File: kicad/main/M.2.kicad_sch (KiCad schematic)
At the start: 10 parts, among them J2 1-2199119-5, M2_ACT1 YLED0603B, Y1 ASEK-32.768KHZ-LRT

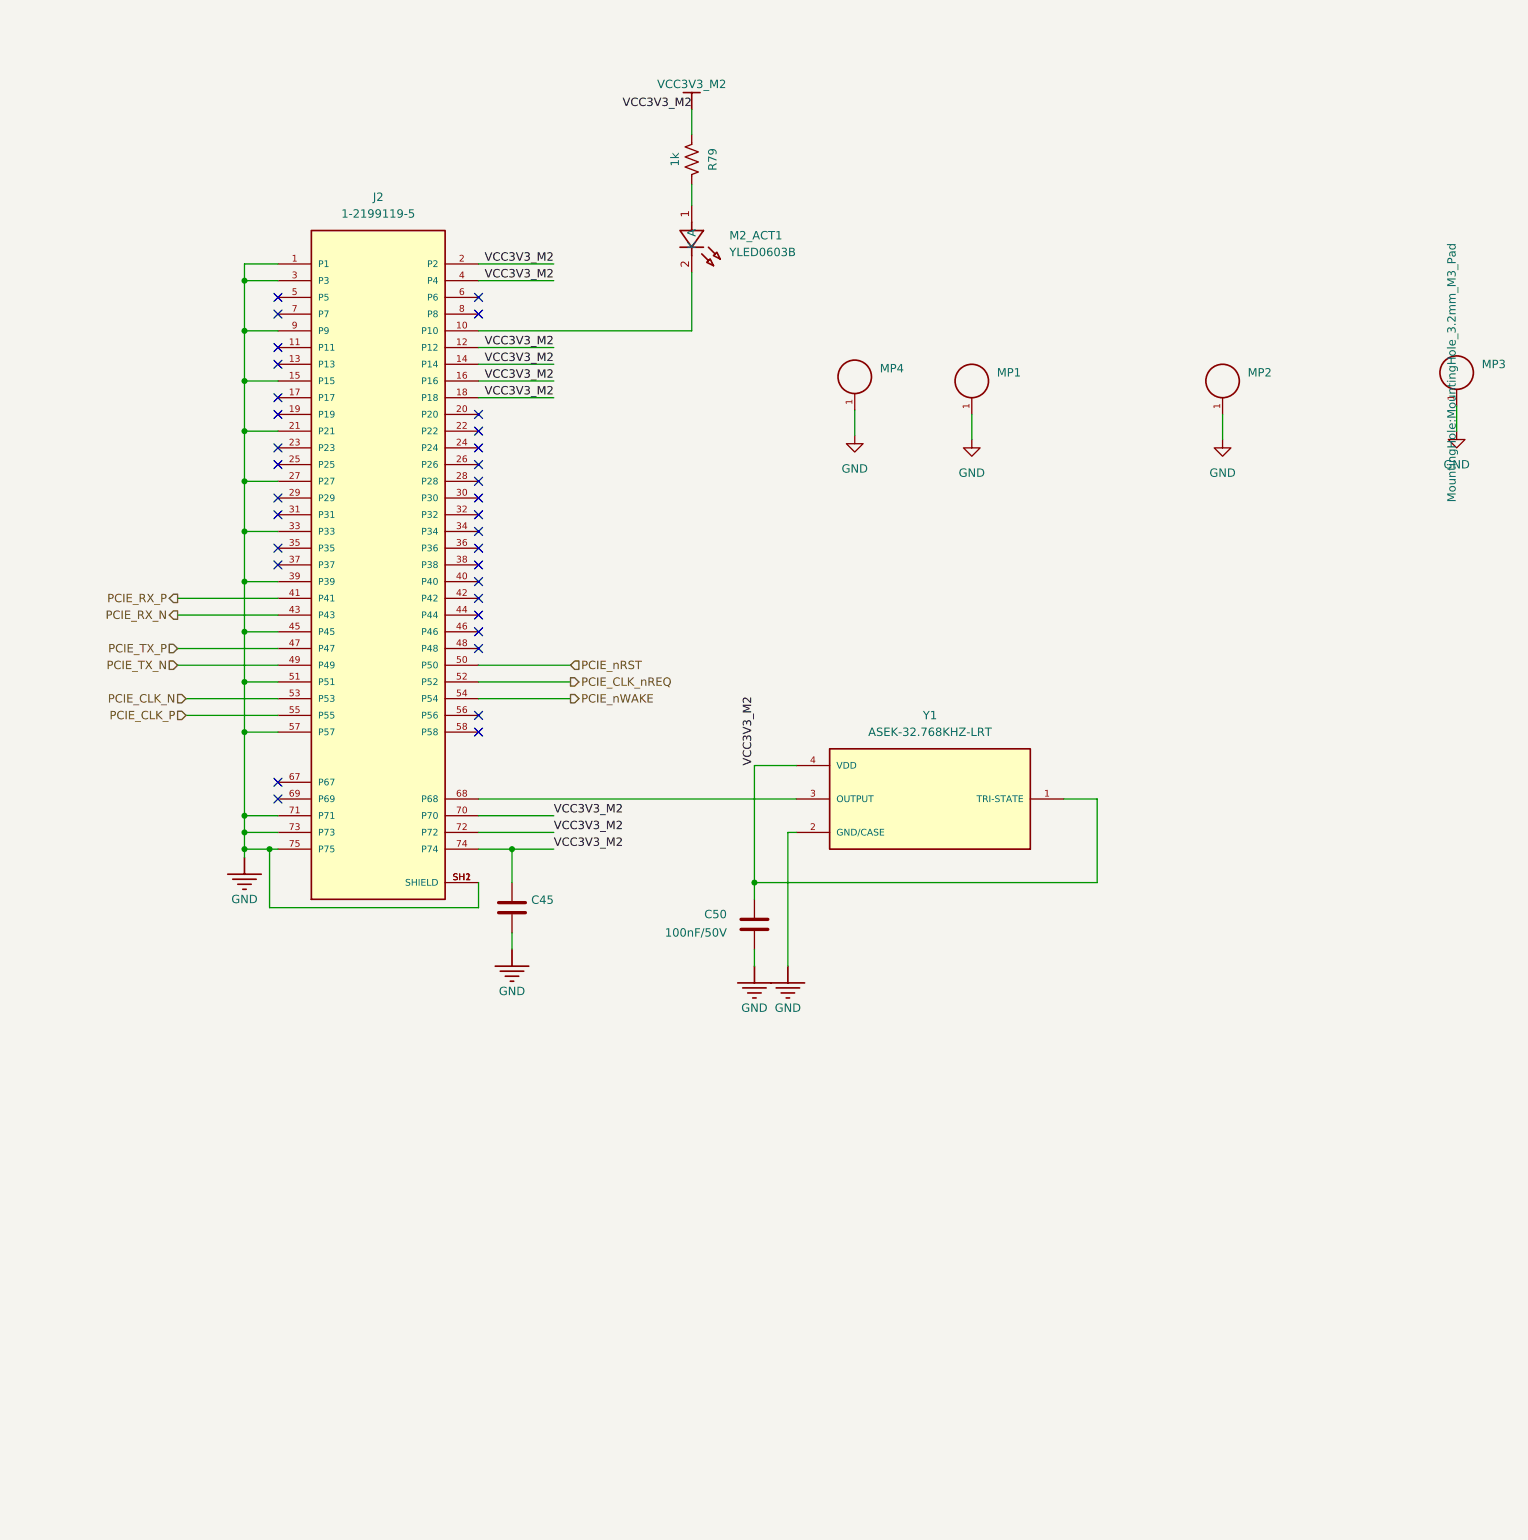
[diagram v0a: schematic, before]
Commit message: Cliff/bumpers connector
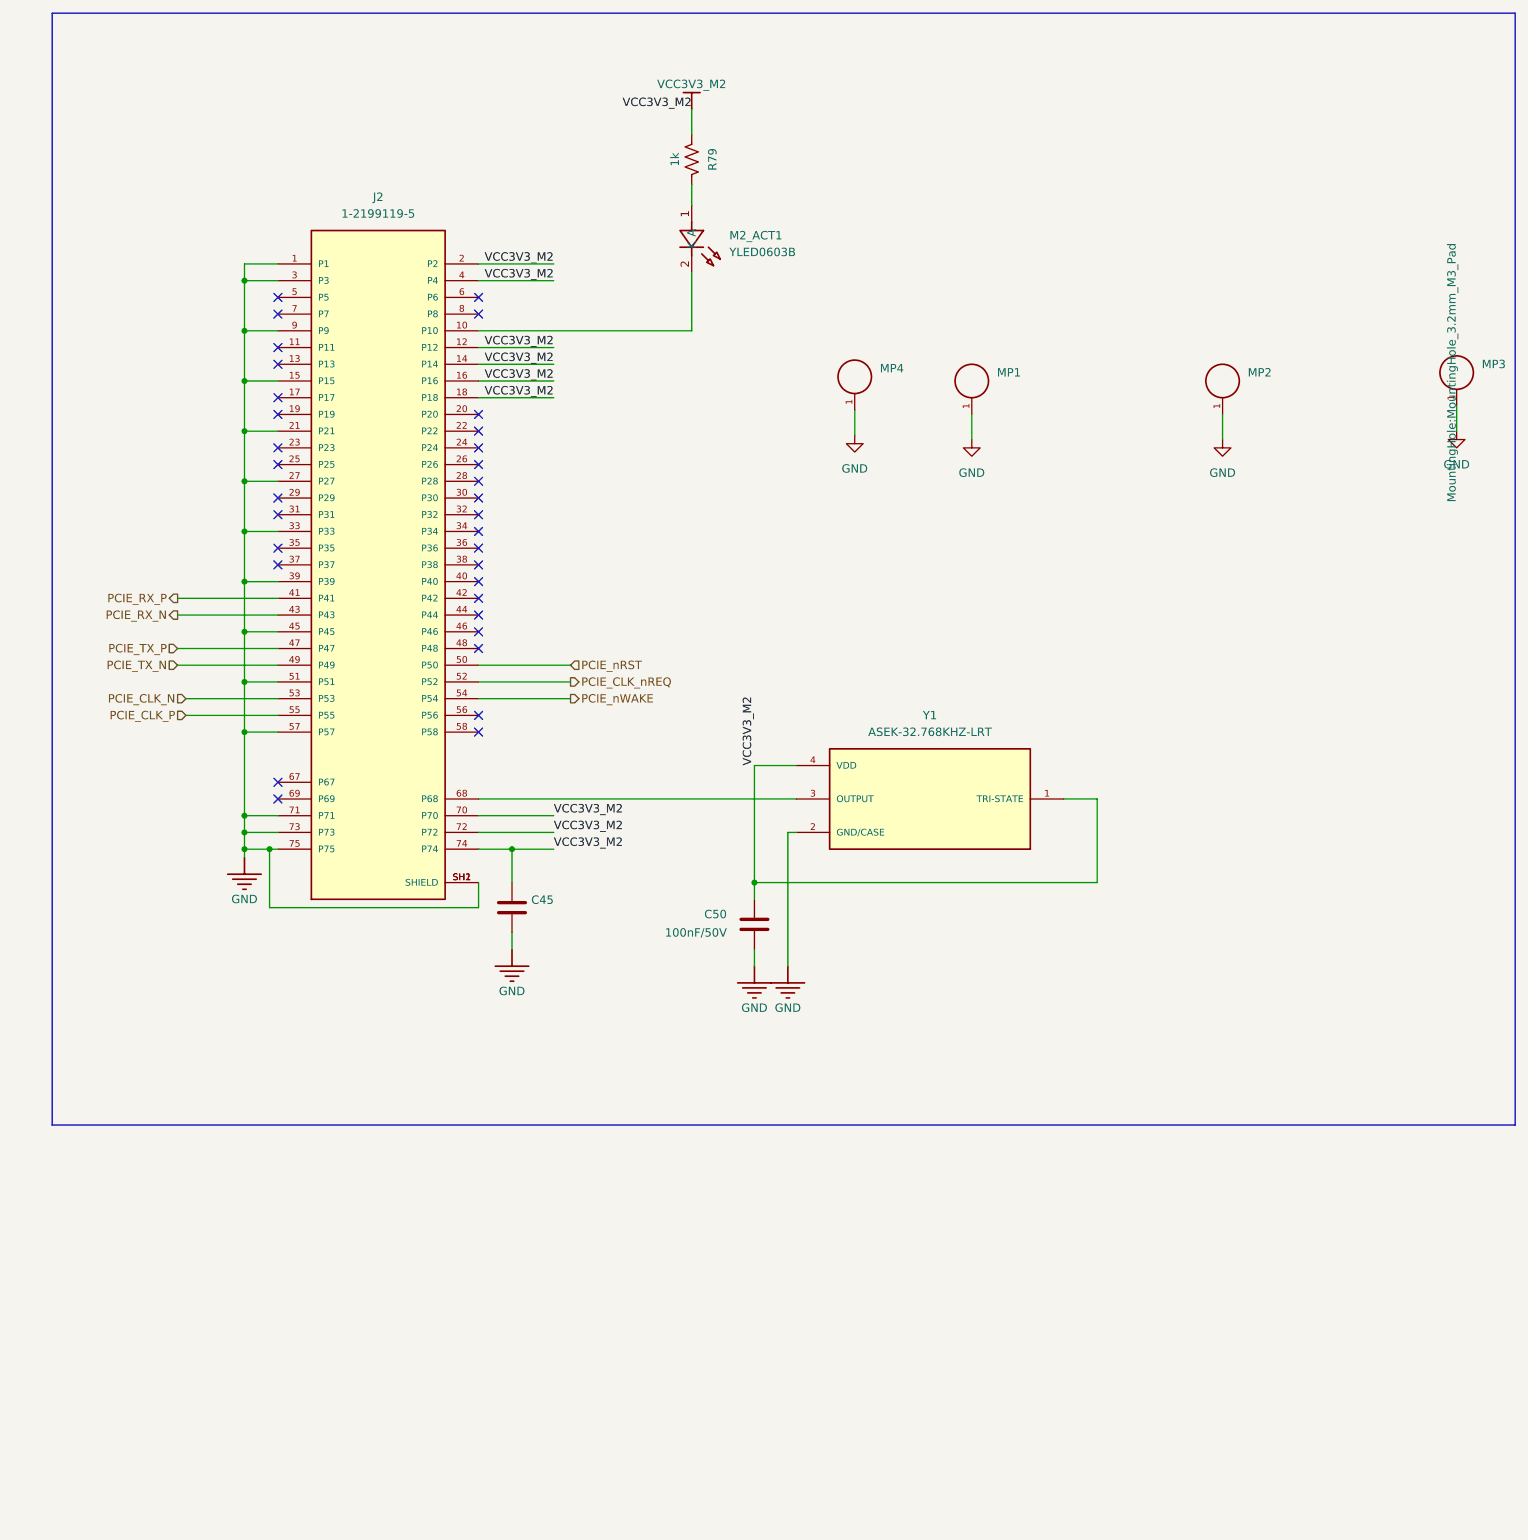
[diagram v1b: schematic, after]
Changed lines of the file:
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@@
 	(generator_version "10.0")
 	(paper "A2")
+	(rectangle
+		(start 166.37 40.64)
+		(end 388.62 209.55)
+		(stroke
+			(width 0)
+			(type solid)
+		)
+		(fill
+			(type color)
+			(color 0 72 0 1)
+		)
+	)
 	(junction
 		(at 273.05 172.72)

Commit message: Second review round
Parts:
- C45, C50, J2, R79, Y1: now not fitted
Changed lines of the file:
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@@
 	(generator_version "10.0")
 	(paper "A2")
-	(rectangle
-		(start 166.37 40.64)
-		(end 388.62 209.55)
-		(stroke
-			(width 0)
-			(type solid)
-		)
-		(fill
-			(type color)
-			(color 0 72 0 1)
-		)
-	)
 	(junction
 		(at 273.05 172.72)
@@
 		(on_board yes)
 		(in_pos_files yes)
-		(dnp no)
+		(dnp yes)
 		(property "Reference" "Y1"
 			(at 299.72 147.32 0)
@@
 		(on_board yes)
 		(in_pos_files yes)
-		(dnp no)
+		(dnp yes)
 		(fields_autoplaced yes)
 		(property "Reference" "J2"
@@
 		(on_board yes)
 		(in_pos_files yes)
-		(dnp no)
+		(dnp yes)
 		(property "Reference" "C50"
 			(at 265.43 177.546 0)
@@
 		(on_board yes)
 		(in_pos_files yes)
-		(dnp no)
+		(dnp yes)
 		(property "Reference" "R79"
 			(at 266.7 62.865 90)
@@
 		(on_board yes)
 		(in_pos_files yes)
-		(dnp no)
+		(dnp yes)
 		(property "Reference" "C45"
 			(at 239.141 175.3616 0)

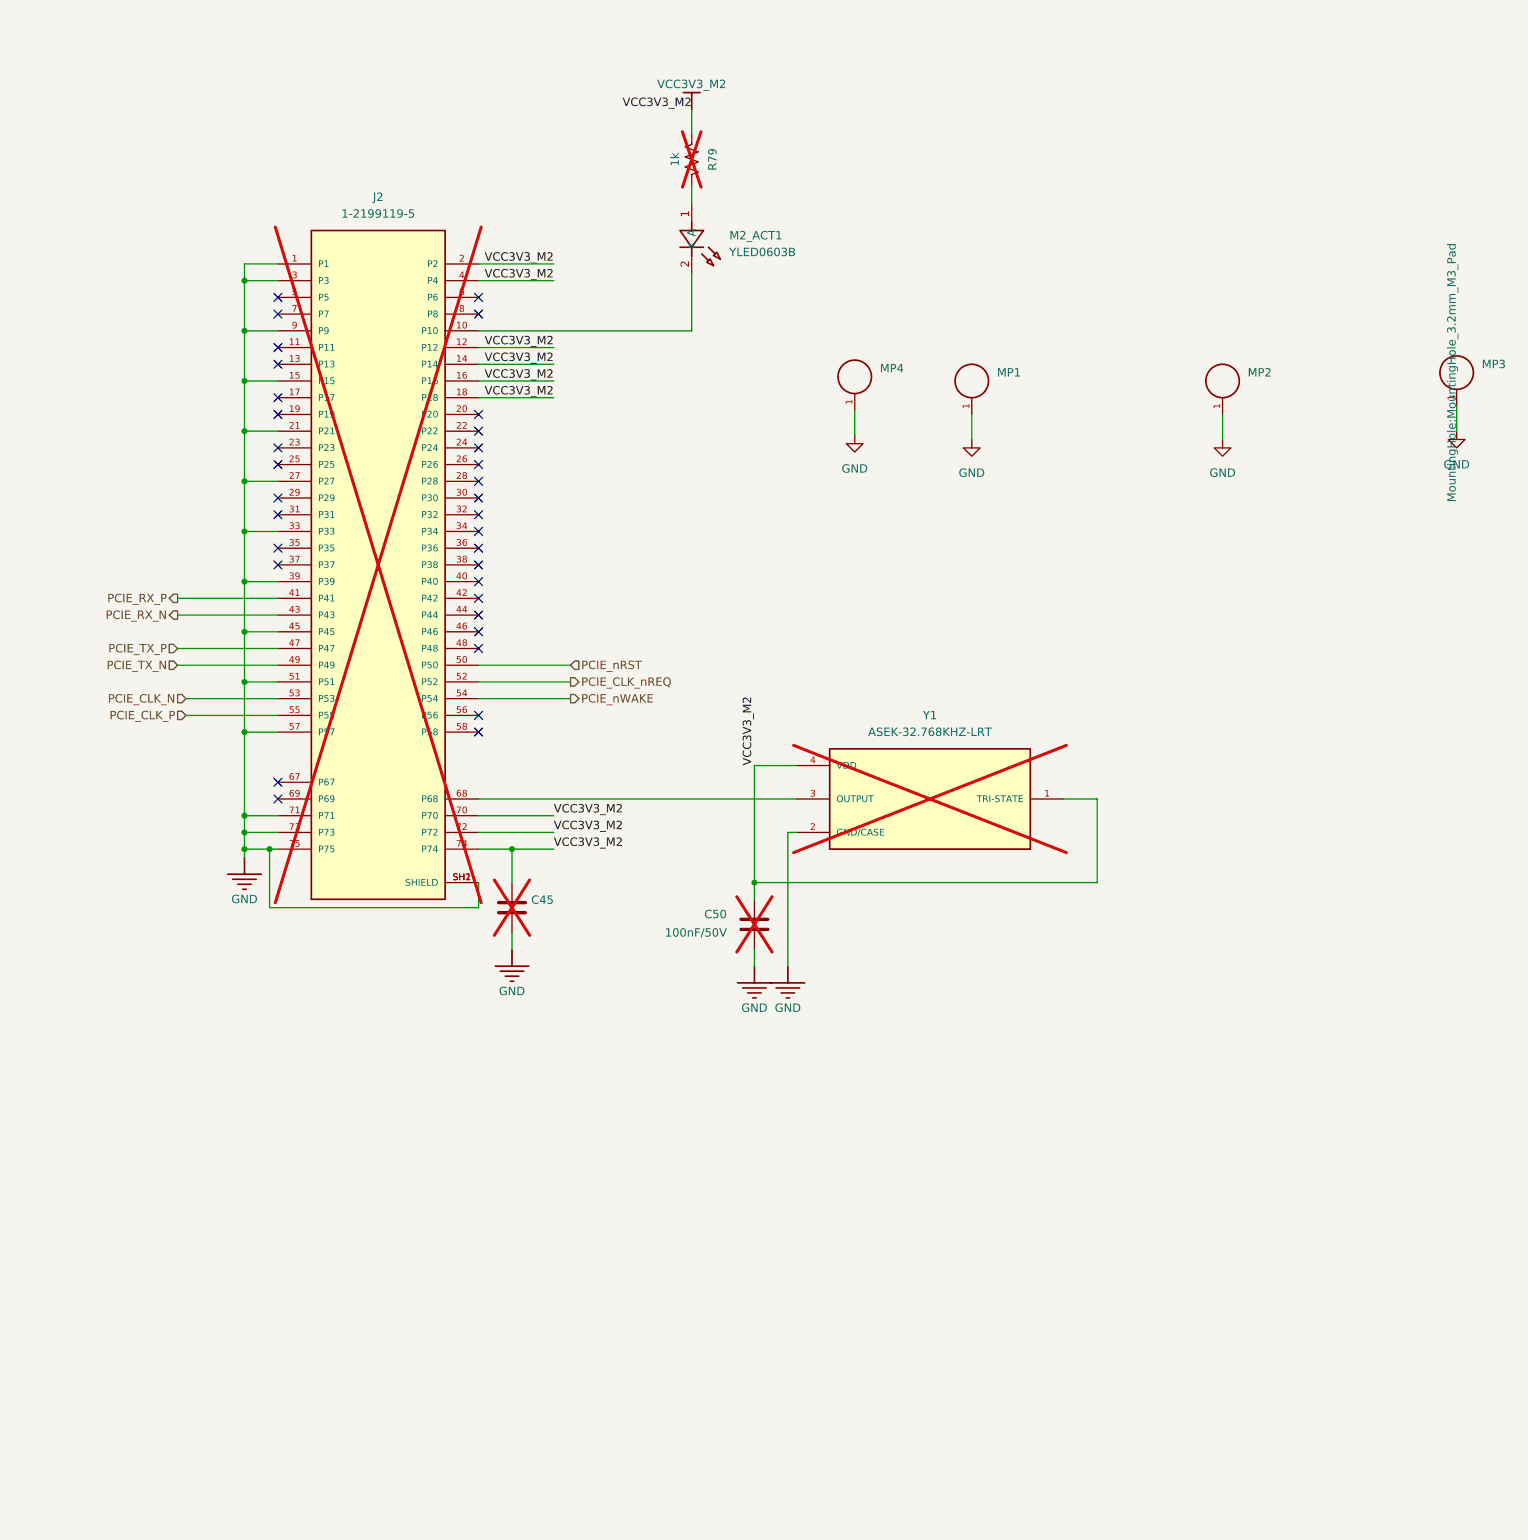
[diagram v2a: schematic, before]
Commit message: Add master fuse
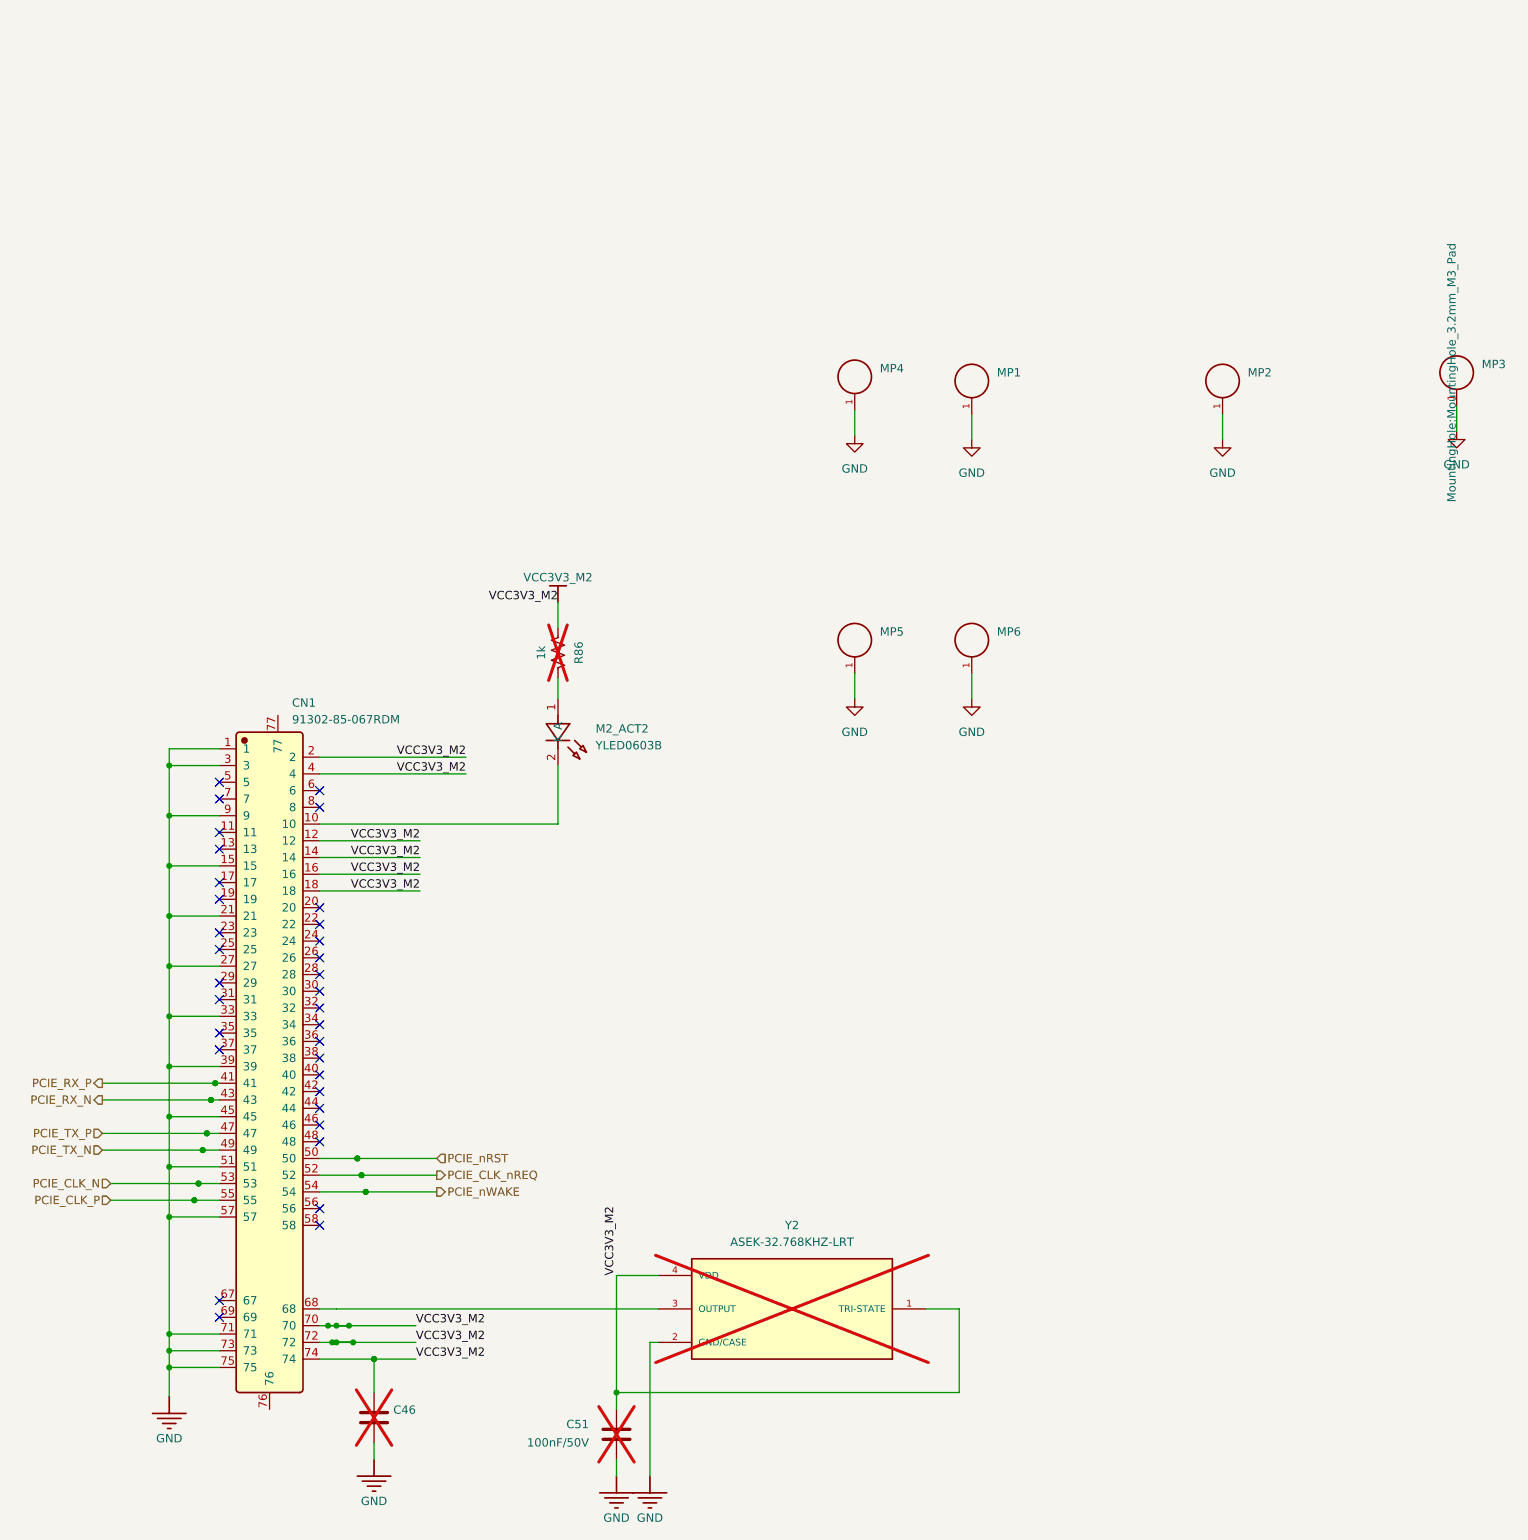
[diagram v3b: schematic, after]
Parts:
- removed C45: 10uF/25V, Capacitor_SMD:C_0603_1608Metric, symbol Library:C
- removed C50: 100nF/50V, Capacitor_SMD:C_0603_1608Metric, symbol Library:C
- removed J2: 1-2199119-5, 1-2199119-5:TE_1-2199119-5, symbol 1-2199119-5:1-2199119-5
- removed M2_ACT1: YLED0603B, JLCImport:YLED0603B, symbol JLCImport:YLED0603B
- removed R79: 1k, Resistor_SMD:R_0603_1608Metric, symbol Device:R_US
- removed Y1: ASEK-32.768KHZ-LRT, ASEK-32.768KHZ-LRT:XTAL_ASEK-32.768KHZ-LRT, symbol ASEK-32.768KHZ-LRT:ASEK-32.768KHZ-LRT
- added C46: 10uF/25V, Capacitor_SMD:C_0603_1608Metric, symbol Library:C
- added C51: 100nF/50V, Capacitor_SMD:C_0603_1608Metric, symbol Library:C
- added CN1: 91302-85-067RDM, JLCImport:91302-85-067RDM, symbol JLCImport:91302-85-067RDM
- added M2_ACT2: YLED0603B, JLCImport:YLED0603B, symbol JLCImport:YLED0603B
- added MP5, MP6: M3 x 1.5mm, MountingHole:MountingHole_3.2mm_M3_Pad, symbol WA-SMSI_9774XXX360:WA-SMSI_9774XXX360
- added R86: 1k, Resistor_SMD:R_0603_1608Metric, symbol Device:R_US
- added Y2: ASEK-32.768KHZ-LRT, ASEK-32.768KHZ-LRT:XTAL_ASEK-32.768KHZ-LRT, symbol ASEK-32.768KHZ-LRT:ASEK-32.768KHZ-LRT
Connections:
- net GND: now also C46.2, C51.2, CN1.1, CN1.15, CN1.21, CN1.27, CN1.3, CN1.33, CN1.39, CN1.45, CN1.51, CN1.57, CN1.71, CN1.73, CN1.75, CN1.9, MP5.1, MP6.1, Y2.2 (GND/CASE)
- net PCIE_CLK_N: now also CN1.53
- net PCIE_CLK_P: now also CN1.55
- net PCIE_CLK_nREQ: now also CN1.52
- net PCIE_RX_N: now also CN1.43
- net PCIE_RX_P: now also CN1.41
- net PCIE_TX_N: now also CN1.49
- net PCIE_TX_P: now also CN1.47
- net PCIE_nRST: now also CN1.50
- net PCIE_nWAKE: now also CN1.54
- net VCC3V3_M2: now also C46.1, C51.1, CN1.12, CN1.14, CN1.16, CN1.18, CN1.2, CN1.4, CN1.74, R86.1, Y2.1 (TRI-STATE), Y2.4 (VDD)
- new net: M2_ACT2.1 (A), R86.2
- new net: CN1.10, M2_ACT2.2 (K)
- new net: CN1.68, Y2.3 (OUTPUT)

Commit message: STM32 power rail switch
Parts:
- C46: Manufacturer_Part_Number GRM21BR61H106KE43L -> (none)
- C51: value 100nF/50V -> 100nF/6.3V; LCSC C1591 -> C5356672; Manufacturer_Part_Number CL10B104KB8NNNC -> (none)
- CN1, M2_ACT2: now not fitted
- R86: LCSC (none) -> C2907113
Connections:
- net GND: now also CN1.76, CN1.77
- net VCC3V3_M2: now also CN1.70, CN1.72
